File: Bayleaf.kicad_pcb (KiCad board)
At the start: 2 copper layers, 137 x 94 mm, 69 parts, among them SW1 SW_SPDT, U1 Nice_Nano_V2

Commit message: v1 power management
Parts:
- removed REF**: JST_SHL_SM02B-SHLS-TF_1x02-1MP_P1.00mm_Horizontal, Connector_JST:JST_SHL_SM02B-SHLS-TF_1x02-1MP_P1.00mm_Horizontal
- added J1 (Battery): Conn_01x02_Socket, Connector_PinHeader_2.54mm:PinHeader_1x02_P2.54mm_Vertical, F.Cu at (118.0, 39.0)
- added J2: Conn_01x02_Socket, Connector_JST:JST_SH_SM02B-SRSS-TB_1x02-1MP_P1.00mm_Horizontal, F.Cu at (116.0, 83.1)
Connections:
- SW1 pad 2: unconnected-(SW1-B-Pad2) -> +BATT
- SW1 pad 3: unconnected-(SW1-C-Pad3) -> Net-(J1-Pin_2)
- U1 pad 23: unconnected-(U1-GND-Pad23) -> GND
- U1 pad 24: unconnected-(U1-B+-Pad24) -> +BATT
- U1 pad 3: unconnected-(U1-GND-Pad3) -> GND
- U1 pad 4: unconnected-(U1-GND-Pad4) -> GND
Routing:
- net +BATT: track 0.00 -> 91.6 mm
- net Net-(J1-Pin_2): track 0.00 -> 52.9 mm, vias 0 -> 2
- net col-3L: track 152.1 -> 153.3 mm
- added copper zone on B.Cu, net GND
- added copper zone on F.Cu, net GND
- removed copper zone on B.Cu, net (none)
- removed copper zone on F.Cu, net (none)

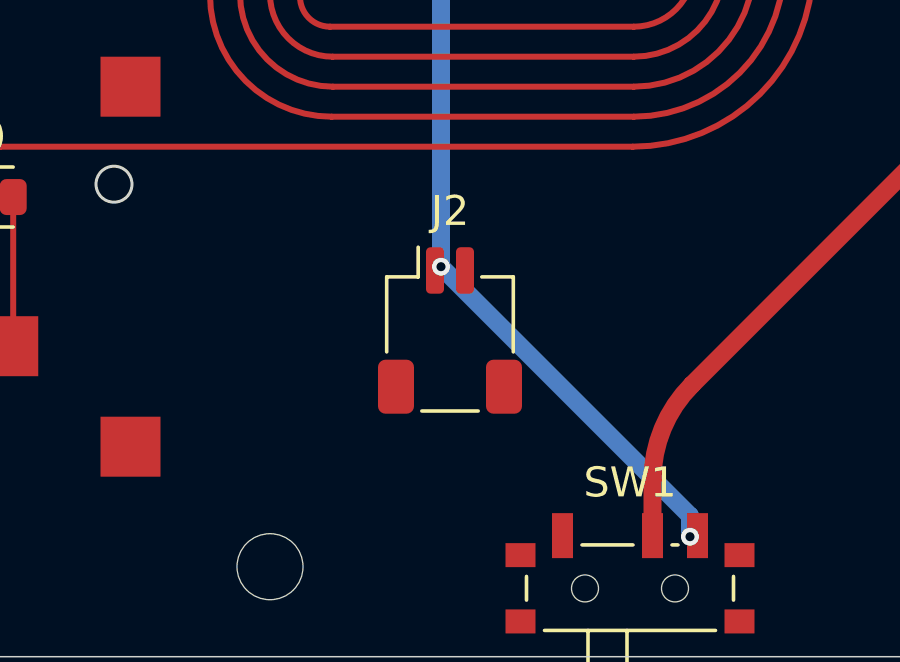
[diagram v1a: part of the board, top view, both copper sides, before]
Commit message: Added jst connector
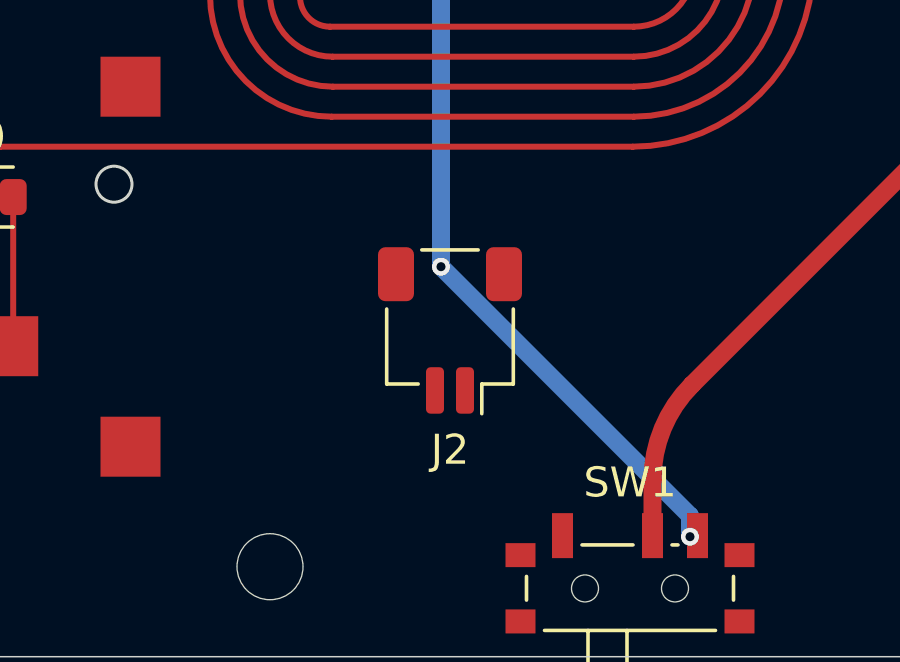
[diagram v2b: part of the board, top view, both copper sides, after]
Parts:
- turned J2 to 180 degrees

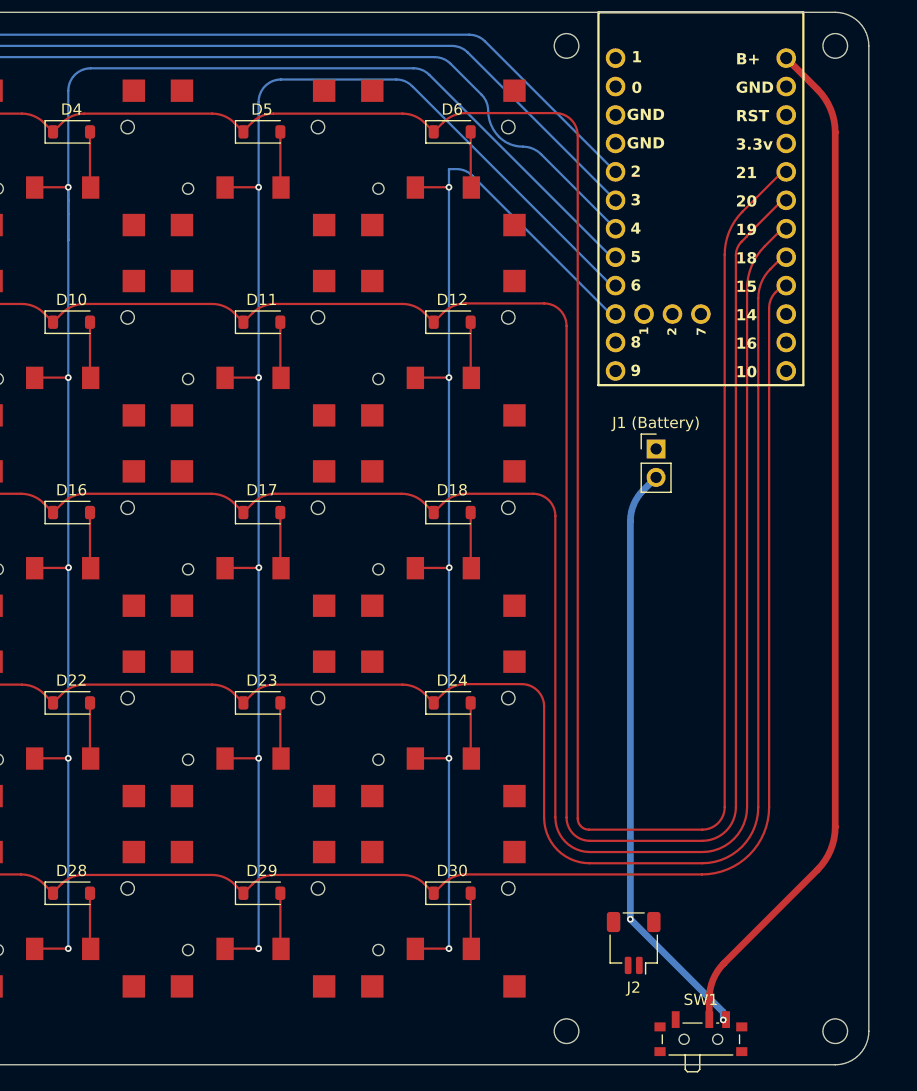
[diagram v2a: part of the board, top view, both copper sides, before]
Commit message: Add rst, flags, logo, mounting hole
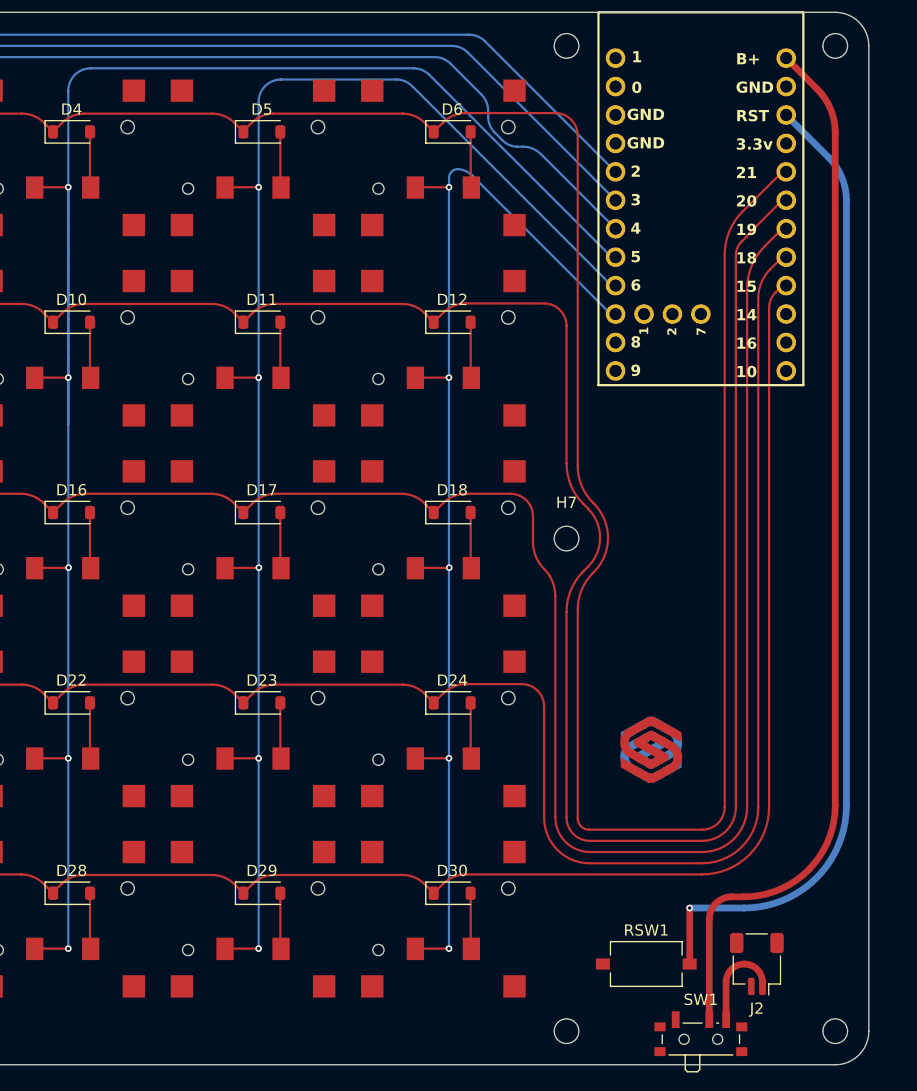
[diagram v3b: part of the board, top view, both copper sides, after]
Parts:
- removed J1 (Battery): Conn_01x02_Socket, Connector_PinHeader_2.54mm:PinHeader_1x02_P2.54mm_Vertical
- added H7: MountingHole, MountingHole:MountingHole_2.2mm_M2, F.Cu at (110.0, 47.0)
- added RSW1: SW_RST, Button_Switch_SMD:SW_Tactile_SPST_NO_Straight_CK_PTS636Sx25SMTRLFS, F.Cu at (117.1, 85.0)
- moved J2 11.2 mm to (127.0, 85.0)
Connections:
- J2 pad 1: Net-(J1-Pin_2) -> +BATT
- SW1 pad 2: +BATT -> RAW
- SW1 pad 3: Net-(J1-Pin_2) -> +BATT
- U1 pad 21: unconnected-(U1-3.3v-Pad21) -> VCC
- U1 pad 22: unconnected-(U1-RST-Pad22) -> RESET
- U1 pad 24: +BATT -> RAW
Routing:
- net RAW: track 0.00 -> 93.9 mm
- net RESET: track 0.00 -> 87.5 mm, vias 0 -> 1
- net +BATT: track 91.6 -> 8.69 mm
- net Net-(J1-Pin_2): track 52.9 -> 0.00 mm, vias 2 -> 0
- net col-3L: track 153.3 -> 169.7 mm
- net row-1L: track 221.5 -> 223.1 mm
- net row-2L: track 203.6 -> 202.1 mm
- net row-0L: track 239.4 -> 240.7 mm

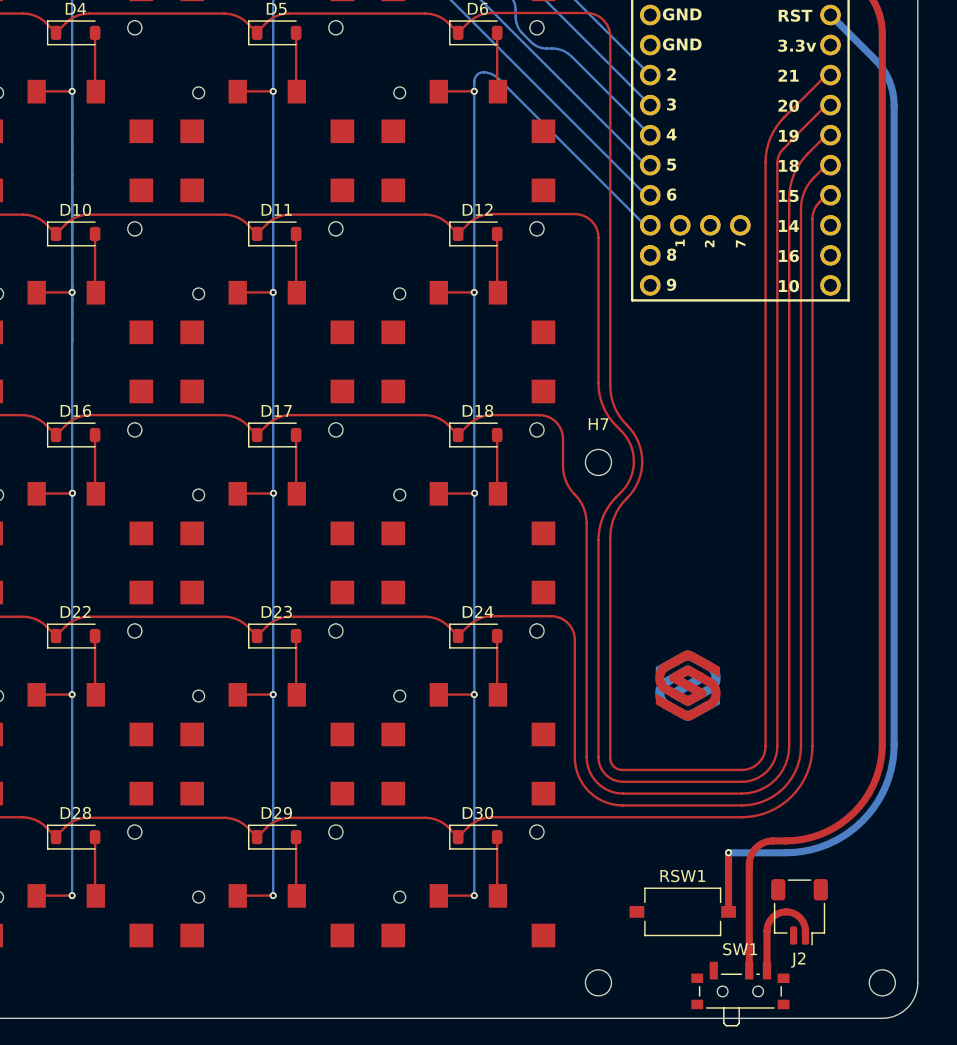
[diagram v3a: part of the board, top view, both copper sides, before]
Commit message: Add case params
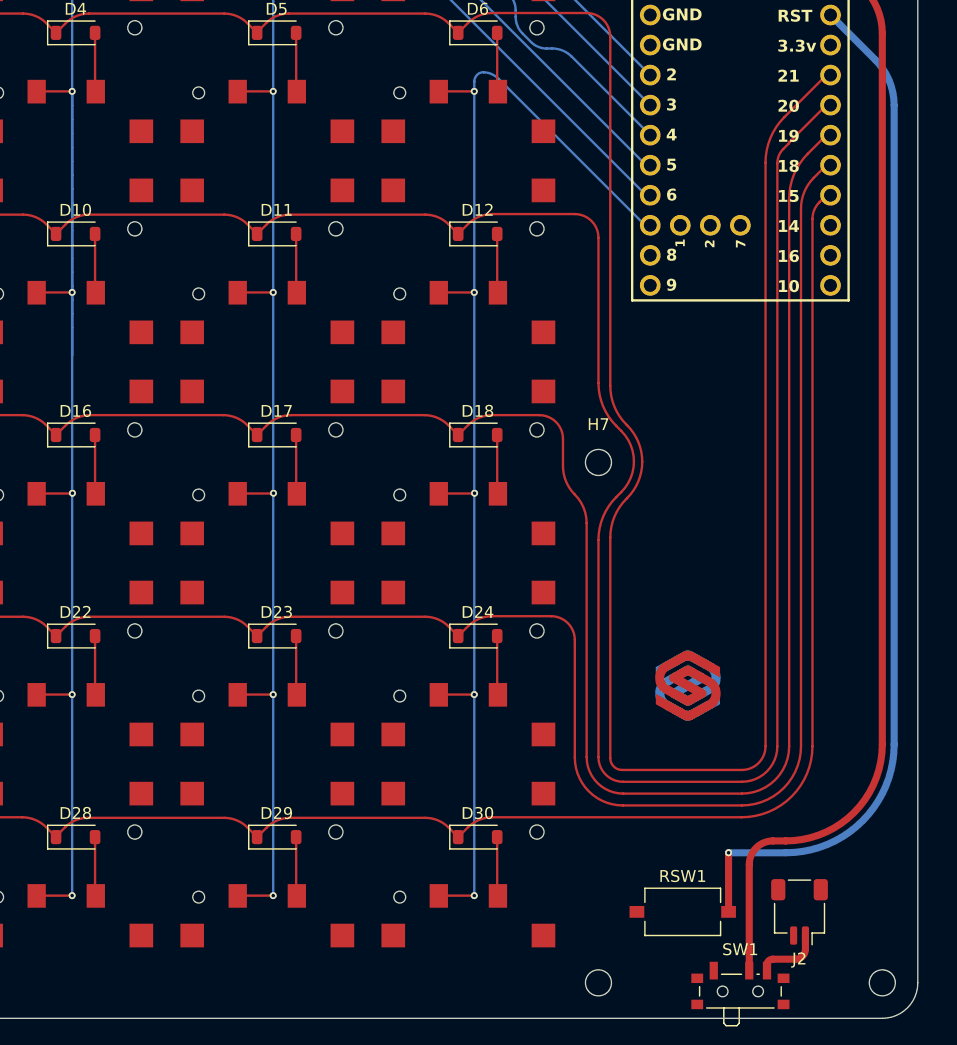
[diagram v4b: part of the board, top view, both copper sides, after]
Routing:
- net +BATT: track 8.69 -> 5.99 mm
- net col-3L: track 169.7 -> 170.8 mm
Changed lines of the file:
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@@
 	)
 	(gr_line
-		(start 107 7)
-		(end 107 89)
+		(start 108 5.5)
+		(end 108 88.5)
+		(stroke
+			(width 0.1)
+			(type default)
+		)
+		(layer "Dwgs.User")
+	)
+	(gr_line
+		(start 135 3.5)
+		(end 135 90.5)
+		(stroke
+			(width 0.1)
+			(type default)
+		)
+		(layer "Dwgs.User")
+	)
+	(gr_arc
+		(start 133.5 2)
+		(mid 134.56066 2.43934)
+		(end 135 3.5)
+		(stroke
+			(width 0.1)
+			(type default)
+		)
+		(layer "Dwgs.User")
+	)
+	(gr_line
+		(start 110 90.5)
+		(end 110 3.5)
+		(stroke
+			(width 0.1)
+			(type default)
+		)
+		(layer "Dwgs.User")
+	)
+	(gr_line
+		(start 133.5 92)
+		(end 111.5 92)
+		(stroke
+			(width 0.1)
+			(type default)
+		)
+		(layer "Dwgs.User")
+	)
+	(gr_line
+		(start 106.5 90)
+		(end 6.5 90)
+		(stroke
+			(width 0.1)
+			(type default)
+		)
+		(layer "Dwgs.User")
+	)
+	(gr_arc
+		(start 6.5 90)
+		(mid 5.43934 89.56066)
+		(end 5 88.5)
 		(stroke
 			(width 0.1)
@@
 	)
 	(gr_arc
-		(start 5 6)
-		(mid 5.585786 4.585786)
-		(end 7 4)
+		(start 135 90.5)
+		(mid 134.56066 91.56066)
+		(end 133.5 92)
+		(stroke
+			(width 0.1)
+			(type default)
+		)
+		(layer "Dwgs.User")
+	)
+	(gr_arc
+		(start 5 5.5)
+		(mid 5.43934 4.43934)
+		(end 6.5 4)
 		(stroke
 			(width 0.1)
@@
 	)
 	(gr_line
-		(start 106 90)
-		(end 7 90)
+		(start 5 88.5)
+		(end 5 5.5)
 		(stroke
 			(width 0.1)
@@
 	)
 	(gr_arc
-		(start 7 90)
-		(mid 5.585786 89.414214)
-		(end 5 88)
+		(start 110 3.5)
+		(mid 110.43934 2.43934)
+		(end 111.5 2)
 		(stroke
 			(width 0.1)
@@
 	)
 	(gr_line
-		(start 5 88)
-		(end 5 6)
+		(start 111.5 2)
+		(end 133.5 2)
 		(stroke
 			(width 0.1)
@@
 	)
 	(gr_arc
-		(start 106 4)
-		(mid 107.414214 4.585786)
-		(end 108 6)
+		(start 111.5 92)
+		(mid 110.43934 91.56066)
+		(end 110 90.5)
 		(stroke
 			(width 0.1)
@@
 	)
 	(gr_arc
-		(start 108 88)
-		(mid 107.414214 89.414214)
-		(end 106 90)
+		(start 108 88.5)
+		(mid 107.56066 89.56066)
+		(end 106.5 90)
 		(stroke
 			(width 0.1)
@@
 	)
 	(gr_line
-		(start 7 4)
-		(end 106 4)
+		(start 6.5 4)
+		(end 106.5 4)
+		(stroke
+			(width 0.1)
+			(type default)
+		)
+		(layer "Dwgs.User")
+	)
+	(gr_arc
+		(start 106.5 4)
+		(mid 107.56066 4.43934)
+		(end 108 5.5)
 		(stroke
 			(width 0.1)
@@
 	)
 	(segment
+		(start 65.5 35.605428)
+		(end 65.5 37.948572)
+		(width 0.2)
+		(layer "B.Cu")
+		(net 39)
+	)
+	(segment
 		(start 65.5 18.015928)
 		(end 65.5 19.191482)
@@
 	)
 	(segment
-		(start 65.5 36.777)
+		(start 65.5 35.605428)
 		(end 65.5 34.433856)
 		(width 0.2)
@@
 	)
 	(segment
+		(start 65.5 37.948572)
+		(end 65.5 35.605428)
+		(width 0.2)
+		(layer "B.Cu")
+		(net 39)
+	)
+	(segment
 		(start 65.5 18.007964)
 		(end 65.5 16.828428)
@@
 	)
 	(segment
-		(start 65.5 83.625)
-		(end 65.5 36.777)
+		(start 65.5 37.948572)
+		(end 65.5 83.625)
 		(width 0.2)
 		(layer "B.Cu")
@@
 	)
 	(segment
-		(start 65.5 34.433856)
-		(end 65.5 36.777)
+		(start 65.5 35.605428)
+		(end 65.5 34.433856)
 		(width 0.2)
 		(layer "B.Cu")
@@
 	)
 	(arc
+		(start 65.5 35.605428)
+		(mid 65.5 35.605428)
+		(end 65.5 35.605428)
+		(width 0.2)
+		(layer "B.Cu")
+		(net 39)
+	)
+	(arc
 		(start 65.5 32.090711)
 		(mid 65.5 32.09071)
@@
 	)
 	(segment
-		(start 100.301502 14.001023)
-		(end 100.302526 14.002047)
+		(start 100.302526 14.002047)
+		(end 100.301502 14.001023)
 		(width 0.2)
 		(layer "B.Cu")
@@
 	)
 	(arc
-		(start 100.299031 14)
+		(start 99.506878 14.792149)
 		(mid 99.738893 14.232015)
-		(end 99.506878 14.792149)
+		(end 100.299031 14)
 		(width 0.2)
 		(layer "B.Cu")
@@
 	)
 	(arc
-		(start 100.301502 14.001023)
+		(start 100.299031 14)
 		(mid 100.300368 14.000265)
-		(end 100.299031 14)
+		(end 100.301502 14.001023)
 		(width 0.2)
 		(layer "B.Cu")
@@
 	)
 	(arc
-		(start 99.506878 15.613258)
+		(start 99.503439 15.621561)
 		(mid 99.505984 15.617751)
-		(end 99.503439 15.621561)
+		(end 99.506878 15.613258)
 		(width 0.2)
 		(layer "B.Cu")
@@
 	)
 	(arc
-		(start 125.830854 79)
+		(start 134 70.830854)
 		(mid 131.607313 76.607313)
-		(end 134 70.830854)
+		(end 125.830854 79)
 		(width 0.6)
 		(layer "F.Cu")
@@
 	)
 	(segment
-		(start 127.5 86.625007)
-		(end 127.5 87)
+		(start 127.5 88.146446)
+		(end 127.5 87.187496)
 		(width 0.6)
 		(layer "F.Cu")
@@
 	)
 	(segment
-		(start 124.25 86.625)
+		(start 124.25 89.482171)
 		(end 124.25 89.964342)
 		(width 0.6)
@@
 		(net 47)
 	)
+	(segment
+		(start 127.5 86.812503)
+		(end 127.5 86.625007)
+		(width 0.6)
+		(layer "F.Cu")
+		(net 47)
+	)
+	(segment
+		(start 126.646446 89)
+		(end 124.732171 89)
+		(width 0.6)
+		(layer "F.Cu")
+		(net 47)
+	)
+	(segment
+		(start 127.5 86.812503)
+		(end 127.5 87.187496)
+		(width 0.6)
+		(layer "F.Cu")
+		(net 47)
+	)
+	(arc
+		(start 127.25 88.75)
+		(mid 126.973087 88.935027)
+		(end 126.646446 89)
+		(width 0.6)
+		(layer "F.Cu")
+		(net 47)
+	)
 	(arc
-		(start 125.875 85)
-		(mid 124.725951 85.475951)
-		(end 124.25 86.625)
+		(start 127.5 88.146446)
+		(mid 127.435027 88.473087)
+		(end 127.25 88.75)
 		(width 0.6)
 		(layer "F.Cu")
@@
 	)
 	(arc
-		(start 127.5 86.625007)
-		(mid 127.024046 85.475954)
-		(end 125.875 85)
+		(start 124.732171 89)
+		(mid 124.391224 89.141224)
+		(end 124.25 89.482171)
 		(width 0.6)
 		(layer "F.Cu")

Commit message: V1 PCB, confirmed working state
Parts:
- moved J2 12.0 mm to (115.0, 86.0)
- moved RSW1 12.0 mm to (129.1, 86.0)
- moved SW1 0.50 mm to (122.0, 91.9)
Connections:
- SW1 pad 2: RAW -> +BATT
- SW1 pad 3: +BATT -> RAW
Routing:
- net RESET: track 87.5 -> 78.0 mm
- net +BATT: track 5.99 -> 8.10 mm
- net col-3L: track 170.8 -> 171.5 mm
